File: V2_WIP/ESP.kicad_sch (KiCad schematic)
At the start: 12 parts, among them J6 USB_B_Micro, U1 NEO-M9N, U12 USBLC6-2SC6

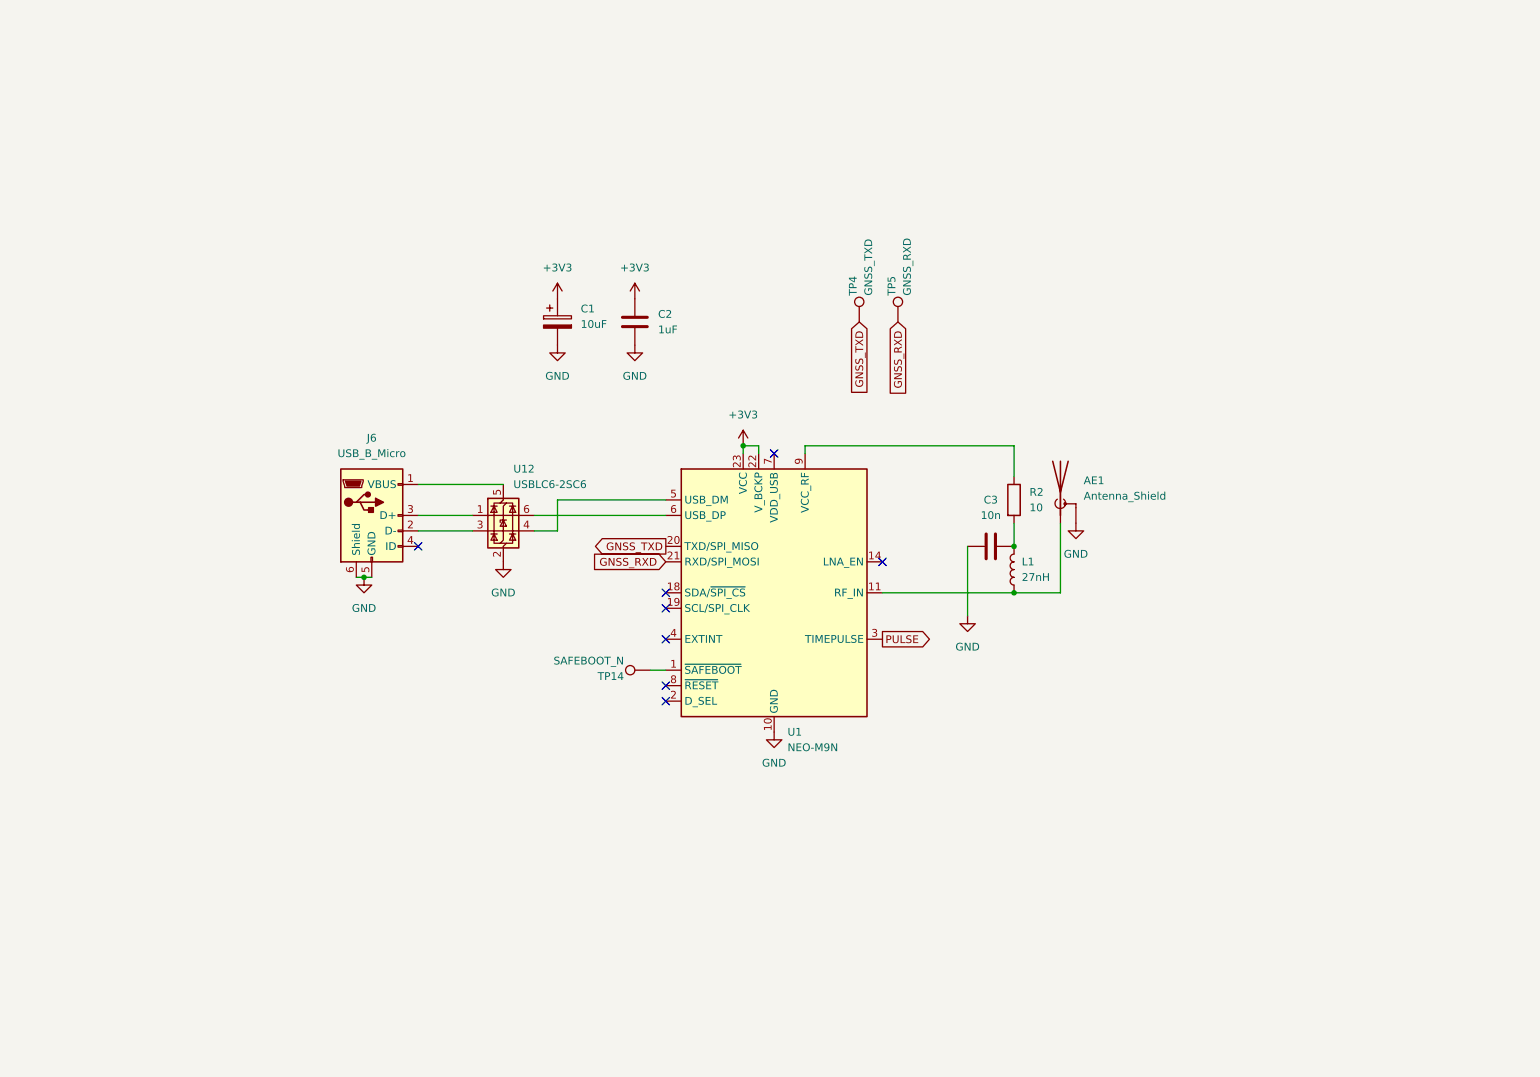
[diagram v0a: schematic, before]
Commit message: Cleaned schematic
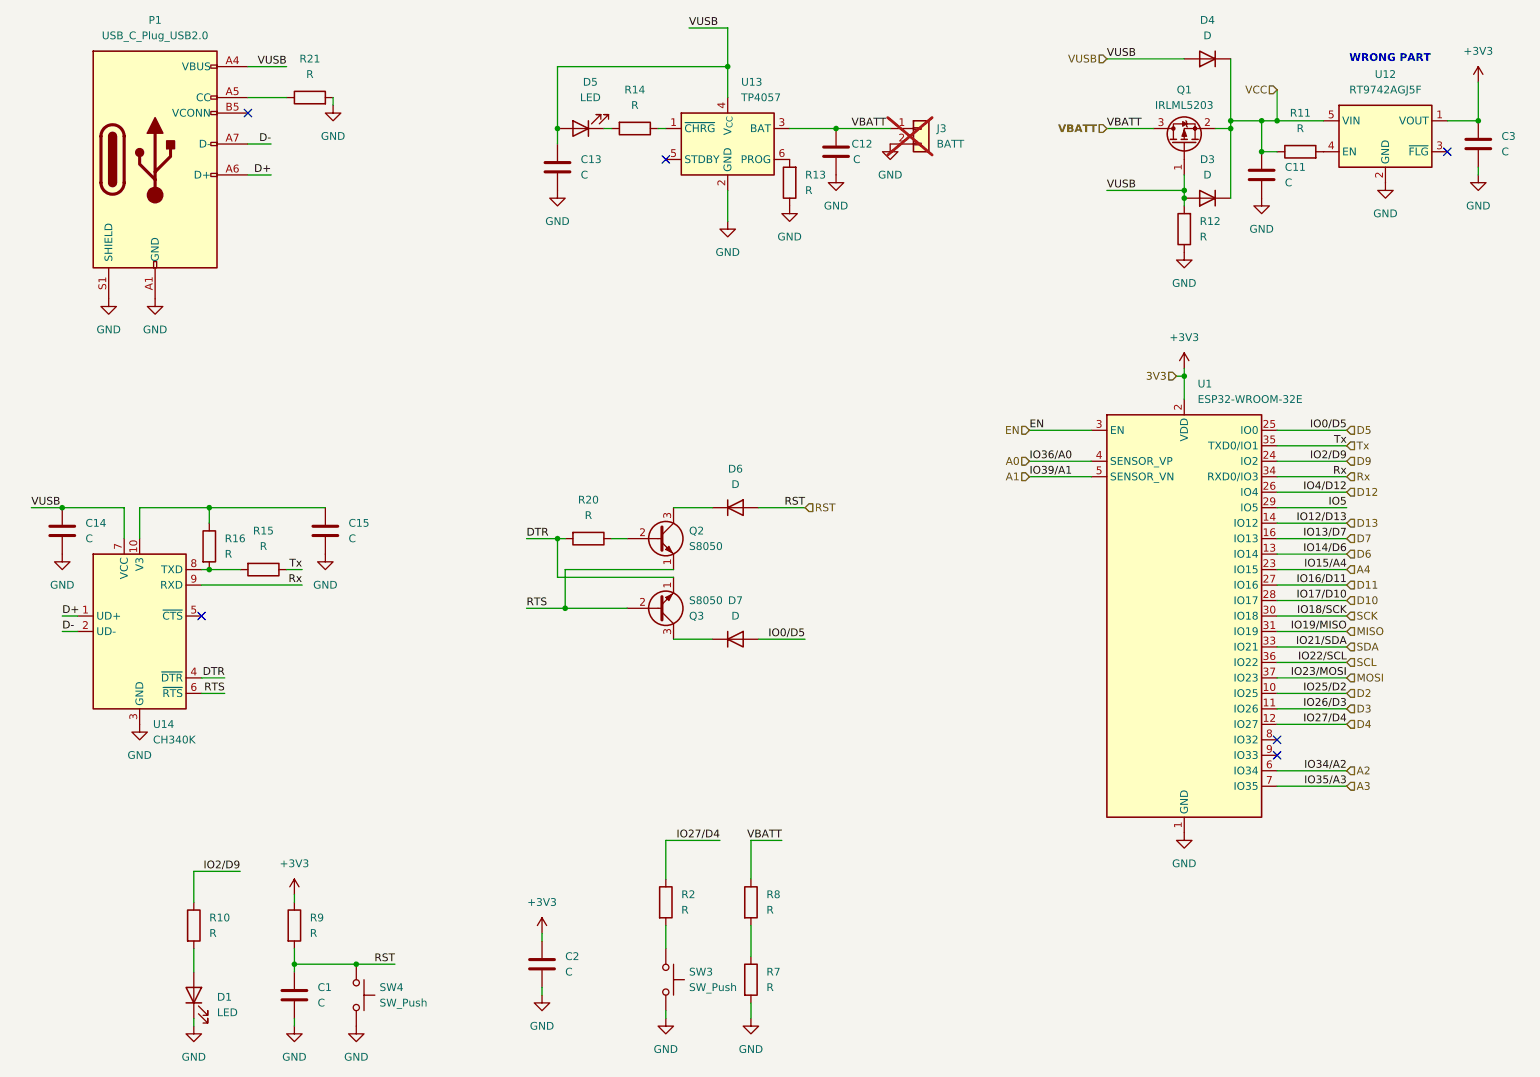
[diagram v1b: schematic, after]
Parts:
- removed AE1: Antenna_Shield, w_conn_rf:lemo_epb00250ntn, symbol Device:Antenna_Shield
- removed C1: 10uF, Capacitor_Tantalum_SMD:CP_EIA-3528-15_AVX-H_Pad1.50x2.35mm_HandSolder, symbol Device:C_Polarized
- removed J6: USB_B_Micro, KiCad:USB3145301A, symbol Connector:USB_B_Micro
- removed L1: 27nH, Inductor_SMD:L_0402_1005Metric_Pad0.77x0.64mm_HandSolder, symbol Device:L
- removed TP14: SAFEBOOT_N, TestPoint:TestPoint_Pad_D1.5mm, symbol Connector:TestPoint
- removed TP4: GNSS_TXD, TestPoint:TestPoint_Pad_D1.5mm, symbol Connector:TestPoint
- removed TP5: GNSS_RXD, TestPoint:TestPoint_Pad_D1.5mm, symbol Connector:TestPoint
- removed U1: NEO-M9N, RF_GPS:ublox_NEO, symbol RF_GPS:NEO-M8N
- removed U12: USBLC6-2SC6, Package_TO_SOT_SMD:SOT-23-6, symbol Power_Protection:USBLC6-2SC6
- added C1, C11, C12, C13, C14, C15: C, Capacitor_SMD:C_0603_1608Metric_Pad1.08x0.95mm_HandSolder, symbol Device:C
- added D1, D5: LED, Diode_SMD:D_0603_1608Metric_Pad1.05x0.95mm_HandSolder, symbol Device:LED
- added D3, D4, D6, D7: D, Diode_SMD:D_0603_1608Metric_Pad1.05x0.95mm_HandSolder, symbol Device:D
- added J3: BATT, 1769:1769, symbol Connector_Generic:Conn_01x02
- added P1: USB_C_Plug_USB2.0, symbol Connector:USB_C_Plug_USB2.0
- added Q1: IRLML5203, Package_TO_SOT_SMD:SOT-23, symbol Transistor_FET:IRLML5203
- added Q2, Q3: S8050, Package_TO_SOT_SMD:SOT-23-3, symbol Transistor_BJT:S8050
- added R10, R11, R12, R13, R14, R15, R16, R20, R21, R7, R8, R9: R, Resistor_SMD:R_0603_1608Metric_Pad0.98x0.95mm_HandSolder, symbol Device:R
- added SW3, SW4: SW_Push, Button_Switch_THT:SW_PUSH_6mm, symbol Switch:SW_Push
- added U1: ESP32-WROOM-32E, RF_Module:ESP32-WROOM-32D, symbol RF_Module:ESP32-WROOM-32E
- added U12: RT9742AGJ5F, Package_TO_SOT_SMD:TSOT-23-5, symbol Power_Management:RT9742AGJ5F
- added U13: TP4057, Package_TO_SOT_SMD:SOT-23-6_Handsoldering, symbol Battery_Management:TP4057
- added U14: CH340K, Package_SO:SSOP-10-1EP_3.9x4.9mm_P1mm_EP2.1x3.3mm, symbol Interface_USB:CH340K
- C2: value 1uF -> C
- C3: value 10n -> C; footprint Capacitor_SMD:C_0805_2012Metric_Pad1.18x1.45mm_HandSolder -> Capacitor_SMD:C_0603_1608Metric_Pad1.08x0.95mm_HandSolder
- R2: value 10 -> R; footprint Resistor_SMD:R_1206_3216Metric_Pad1.30x1.75mm_HandSolder -> Resistor_SMD:R_0603_1608Metric_Pad0.98x0.95mm_HandSolder
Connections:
- net +3V3: now also C3.1, R9.1, U1.2 (VDD), U12.1 (VOUT)
- net GND: now also C3.2, C1.2, C11.2, C12.2, C13.2, C14.2, C15.2, D1.1 (K), J3.2 (Pin_2), P1.A1 (GND), P1.A12 (GND), P1.B1 (GND), P1.B12 (GND), P1.S1 (SHIELD), R12.1, R13.1, R21.2, R7.2, SW3.2, SW4.2, U1.1 (GND), U1.15 (GND), U1.38 (GND), U1.39 (GND), U12.2 (GND), U13.2 (GND), U14.11 (GND), U14.3 (GND); no longer C3.1
- net at R2.2: now also SW3.1; no longer C3.2
- net D4: now reaches R2.1
- net D4: now also U1.12 (IO27)
- new net: C15.1, R16.1, U14.10 (V3)
- new net: D7.1 (K), Q3.3 (C)
- new net: P1.A5 (CC), R21.1
- new net: R11.2, U12.4 (EN)
- new net: Q2.2 (B), R20.1
- new net: D5.1 (K), R14.2
- new net: D1.2 (A), R10.2
- new net: R7.1, R8.2
- new net: R14.1, U13.1 (~{CHRG})
- new net: R13.2, U13.6 (PROG)
- new net: D6.1 (K), Q2.3 (C)
- new net: R15.2, R16.2, U14.8 (TXD)
- new net A0: U1.4 (SENSOR_VP)
- new net A1: U1.5 (SENSOR_VN)
- new net A2: U1.6 (IO34)
- new net A3: U1.7 (IO35)
- new net A4: U1.23 (IO15)
- new net D+: P1.A6 (D+), U14.1 (UD+)
- new net D-: P1.A7 (D-), U14.2 (UD-)
- new net D10: U1.28 (IO17)
- new net D11: U1.27 (IO16)
- new net D12: U1.26 (IO4)
- new net D13: U1.14 (IO12)
- new net D2: U1.10 (IO25)
- new net D3: U1.11 (IO26)
- new net D5: D7.2 (A), U1.25 (IO0)
- new net D6: U1.13 (IO14)
- new net D7: U1.16 (IO13)
- new net D9: R10.1, U1.24 (IO2)
- new net DTR: Q3.1 (E), R20.2, U14.4 (~{DTR})
- new net EN: U1.3 (EN)
- new net IO5: U1.29 (IO5)
- new net MISO: U1.31 (IO19)
- new net MOSI: U1.37 (IO23)
- new net RST: C1.1, D6.2 (A), R9.2, SW4.1
- new net RTS: Q2.1 (E), Q3.2 (B), U14.6 (~{RTS})
- new net Rx: U1.34 (RXD0/IO3), U14.9 (RXD)
- new net SCK: U1.30 (IO18)
- new net SCL: U1.36 (IO22)
- new net SDA: U1.33 (IO21)
- new net Tx: R15.1, U1.35 (TXD0/IO1)
- new net VBATT: C12.1, J3.1 (Pin_1), Q1.3 (D), R8.1, U13.3 (BAT)
- new net VCC: C11.1, D3.1 (K), D4.1 (K), Q1.2 (S), R11.1, U12.5 (VIN)
- new net VUSB: C13.1, C14.1, D3.2 (A), D4.2 (A), D5.2 (A), P1.A4 (VBUS), P1.A9 (VBUS), P1.B4 (VBUS), P1.B9 (VBUS), Q1.1 (G), R12.2, U13.4 (V_{CC}), U14.7 (VCC)
- no-connect marks 8 -> 6
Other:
- note added: "WRONG PART"
- title: GNSS_Geret -> (none)

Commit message: added LED indicators, light sensor, changed to CC 7seg displays
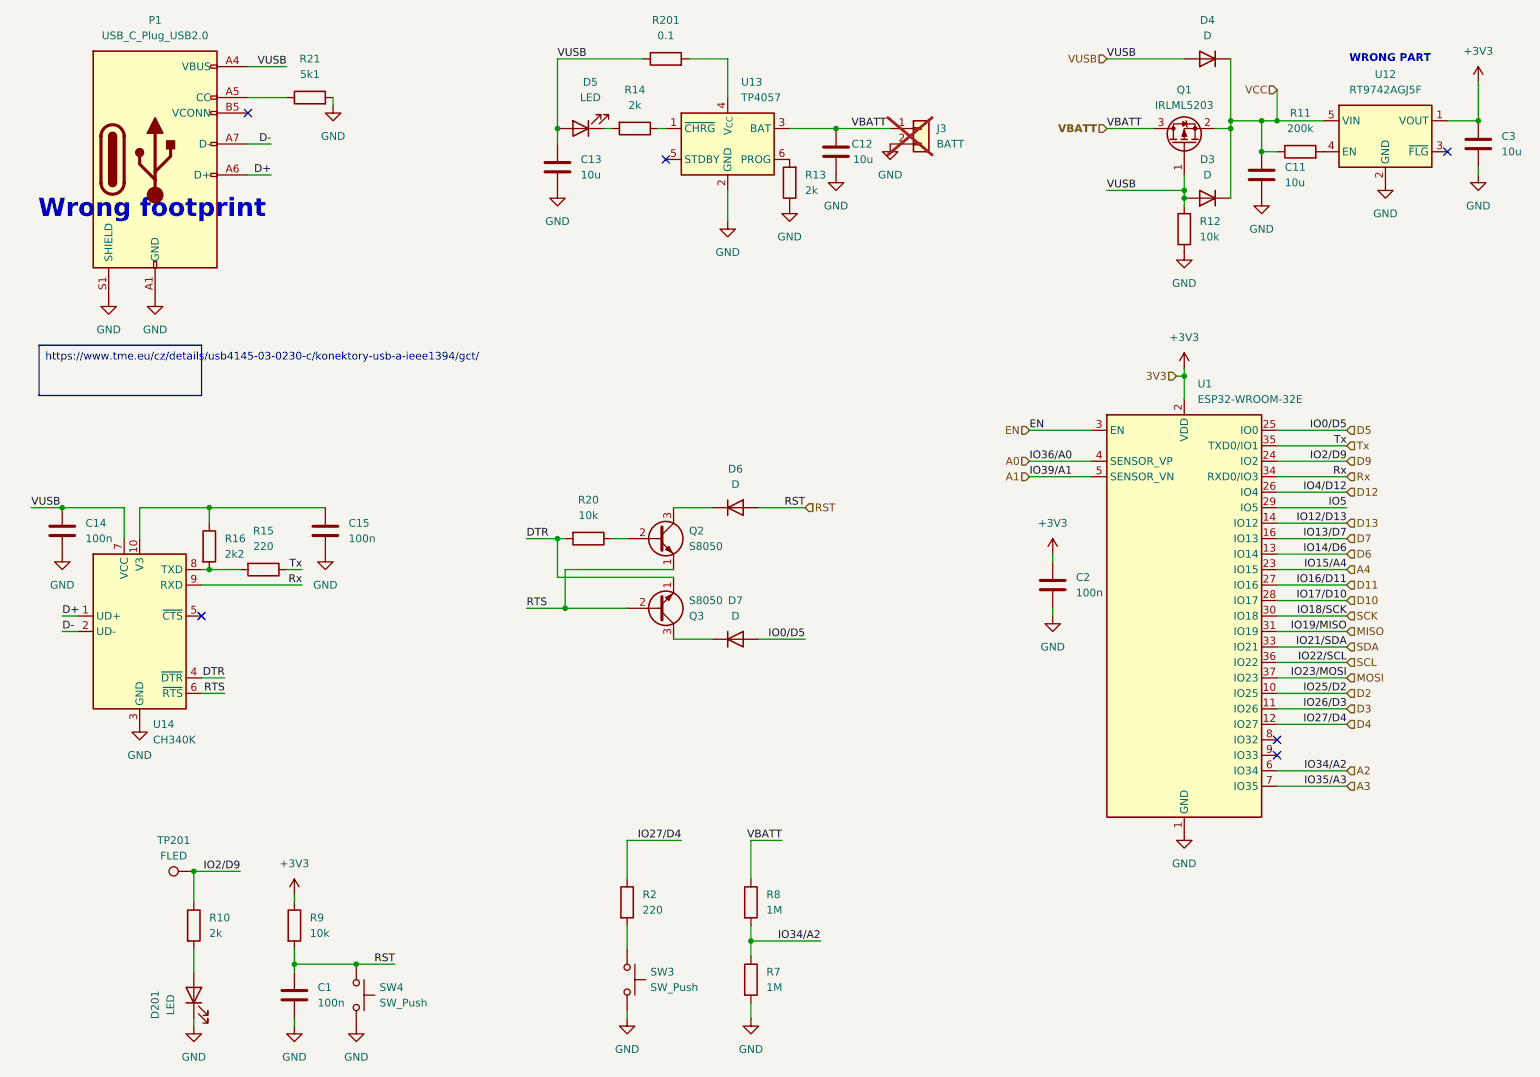
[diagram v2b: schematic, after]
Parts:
- removed D1: LED, Diode_SMD:D_0603_1608Metric_Pad1.05x0.95mm_HandSolder, symbol Device:LED
- added D201: LED, LED_THT:LED_D3.0mm, symbol Device:LED
- added R201: 0.1, Resistor_SMD:R_0603_1608Metric_Pad0.98x0.95mm_HandSolder, symbol Device:R
- added TP201: FLED, TestPoint:TestPoint_Pad_D1.5mm, symbol Connector:TestPoint
- C1, C14, C15, C2: value C -> 100n
- C11, C12, C13, C3: value C -> 10u
- P1: footprint (none) -> Connector_USB:USB_C_Receptacle_G-Switch_GT-USB-7051x
- R10, R13, R14: value R -> 2k
- R11: value R -> 200k
- R12, R20, R9: value R -> 10k
- R15, R2: value R -> 220
- R16: value R -> 2k2
- R21: value R -> 5k1
- R7, R8: value R -> 1M
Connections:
- net A2: now also R7.1, R8.2
- net D9: now also TP201.1
- net GND: now also D201.1 (K)
- net VUSB: now also R201.1; no longer U13.4 (V_{CC})
- net at R10.2: now also D201.2 (A)
- new net: R201.2, U13.4 (V_{CC})
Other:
- note added: "Wrong footprint"
- moved on the sheet: C2, R2, SW3
